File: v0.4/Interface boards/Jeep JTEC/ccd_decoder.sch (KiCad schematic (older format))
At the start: 10 parts, among them Q1 AO3400, Q2 IRF7317

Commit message: Draw Jeep igniters and cruise control drivers
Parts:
- added C? (x2): 3.3n, symbol Device:C
- added JP? (x2): NO, symbol Device:Jumper_NO_Small
- added R? (x2): 10, symbol Device:R
- added R? (x2): 13k, symbol Device:R
- added R?: 120, symbol Device:R
- added U?: USBLC6-2P6, Package_TO_SOT_SMD:SOT-666, symbol Power_Protection:USBLC6-2P6
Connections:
- net CCD+: now also JP?.2, U?.6 (I/O1)
- net CCD-: now also JP?.2, U?.4 (I/O2)
- net CCD_SAFE+: now also C?.1, R?.2
- net CCD_SAFE-: now also C?.1, R?.1
- net GNDA: now also C?.2, C?.2, R?.2, U?.2 (GND)
- net VDDA: now also R?.1, U?.5 (VBUS)
- new net: R?.1, U?.1 (I/O1)
- new net: R?.2, U?.3 (I/O2)
- new net: JP?.1, R?.1, R?.2 (x2)
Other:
- note added: "CCD Termination"
- moved on the sheet: C?, R?, U?A, U?C

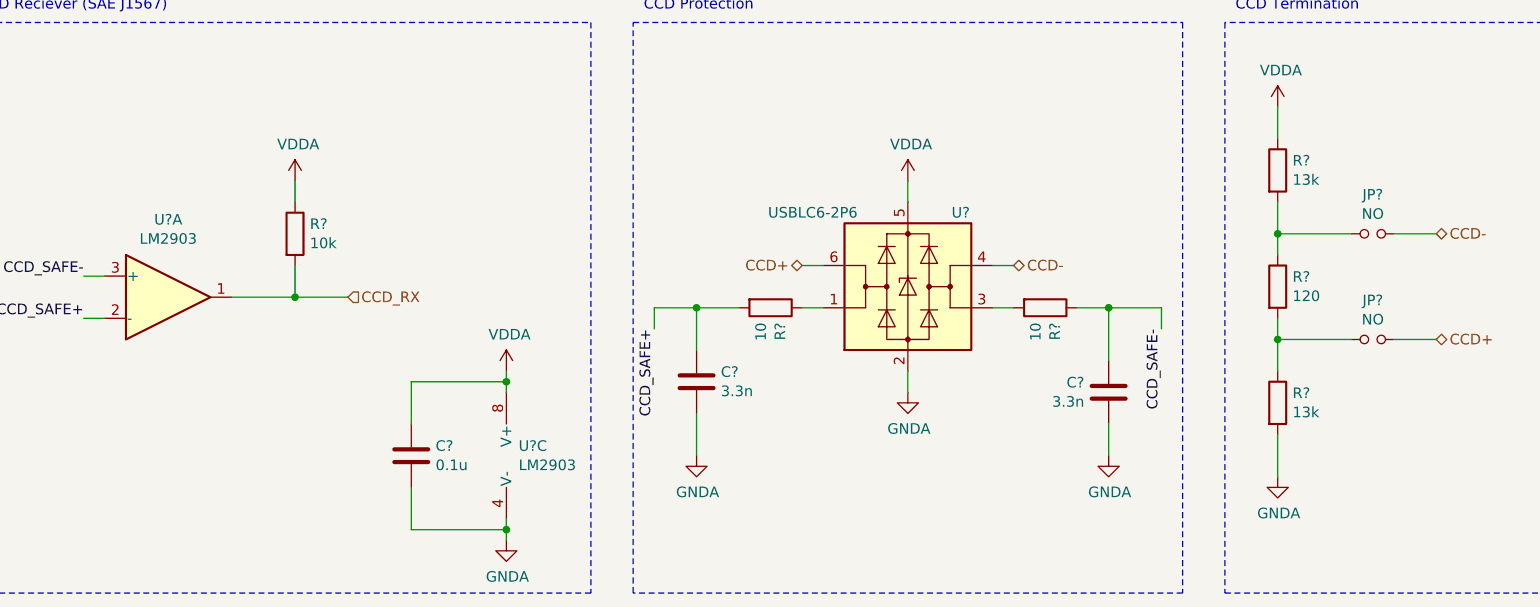
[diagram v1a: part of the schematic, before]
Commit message: Add voltage sense circuit for alternator control
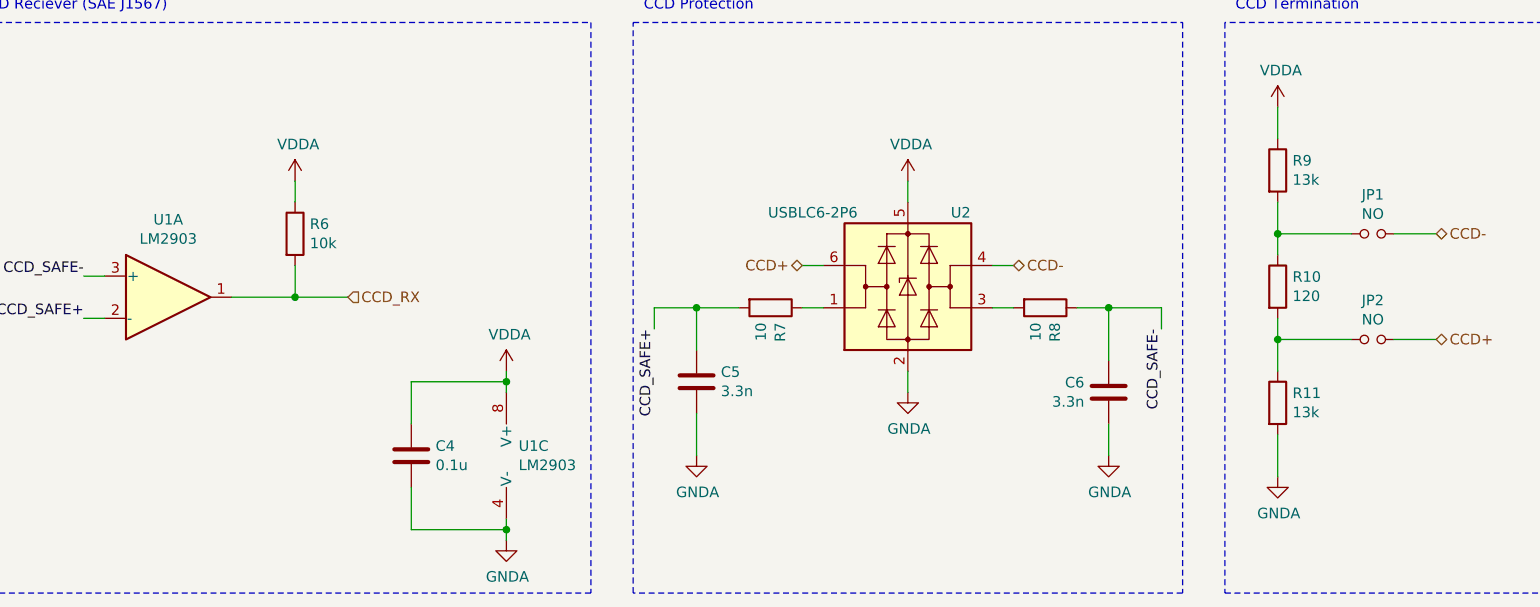
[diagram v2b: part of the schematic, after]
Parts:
- C4, C5, C6: renamed from C?; footprint (none) -> Capacitor_SMD:C_0805_2012Metric
- JP1, JP2: renamed from JP?; footprint (none) -> Connector_PinHeader_2.54mm:PinHeader_1x02_P2.54mm_Vertical
- R1, R2, R3, R4: footprint (none) -> Resistor_SMD:R_0805_2012Metric
- R10, R11, R6, R7, R8, R9: renamed from R?; footprint (none) -> Resistor_SMD:R_0805_2012Metric
- U1: renamed from U?; footprint (none) -> Package_SO:SOIC-8_3.9x4.9mm_P1.27mm; Manufacturer (none) -> onsemi; Manufacturer# (none) -> LM2903DR2G; digikey# (none) -> LM2903DR2GOSCT-ND
- gave numbers to parts that had none: 1
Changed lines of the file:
@@
 F 0 "R1" H 1220 1396 50  0000 L CNN
 F 1 "10k" H 1220 1305 50  0000 L CNN
-F 2 "" V 1080 1350 50  0001 C CNN
+F 2 "Resistor_SMD:R_0805_2012Metric" V 1080 1350 50  0001 C CNN
 F 3 "~" H 1150 1350 50  0001 C CNN
 	1    1150 1350
@@
 F 0 "R2" H 1770 2146 50  0000 L CNN
 F 1 "10k" H 1770 2055 50  0000 L CNN
-F 2 "" V 1630 2100 50  0001 C CNN
+F 2 "Resistor_SMD:R_0805_2012Metric" V 1630 2100 50  0001 C CNN
 F 3 "~" H 1700 2100 50  0001 C CNN
 	1    1700 2100
@@
 F 0 "R3" V 2600 1900 50  0000 C CNN
 F 1 "360" V 2500 1900 50  0000 C CNN
-F 2 "" V 2530 1900 50  0001 C CNN
+F 2 "Resistor_SMD:R_0805_2012Metric" V 2530 1900 50  0001 C CNN
 F 3 "~" H 2600 1900 50  0001 C CNN
 	1    2600 1900
@@
 F 0 "R4" V 2600 2100 50  0000 C CNN
 F 1 "360" V 2500 2100 50  0000 C CNN
-F 2 "" V 2530 2100 50  0001 C CNN
+F 2 "Resistor_SMD:R_0805_2012Metric" V 2530 2100 50  0001 C CNN
 F 3 "~" H 2600 2100 50  0001 C CNN
 	1    2600 2100
@@
 CCD Reciever (SAE J1567)
 $Comp
-L Comparator:LM2903 U?
+L Comparator:LM2903 U1
 U 1 1 61616774
 P 4550 2000
-F 0 "U?" H 4550 2367 50  0000 C CNN
+F 0 "U1" H 4550 2367 50  0000 C CNN
 F 1 "LM2903" H 4550 2276 50  0000 C CNN
-F 2 "" H 4550 2000 50  0001 C CNN
+F 2 "Package_SO:SOIC-8_3.9x4.9mm_P1.27mm" H 4550 2000 50  0001 C CNN
 F 3 "http://www.ti.com/lit/ds/symlink/lm393.pdf" H 4550 2000 50  0001 C CNN
+F 4 "onsemi" H 4550 2000 50  0001 C CNN "Manufacturer"
+F 5 "LM2903DR2G" H 4550 2000 50  0001 C CNN "Manufacturer#"
+F 6 "LM2903DR2GOSCT-ND" H 4550 2000 50  0001 C CNN "digikey#"
 	1    4550 2000
 	1    0    0    -1
 $EndComp
 $Comp
-L Comparator:LM2903 U?
+L Comparator:LM2903 U1
 U 3 1 61617337
 P 6250 2750
-F 0 "U?" H 6208 2796 50  0000 L CNN
+F 0 "U1" H 6208 2796 50  0000 L CNN
 F 1 "LM2903" H 6208 2705 50  0000 L CNN
-F 2 "" H 6250 2750 50  0001 C CNN
+F 2 "Package_SO:SOIC-8_3.9x4.9mm_P1.27mm" H 6250 2750 50  0001 C CNN
 F 3 "http://www.ti.com/lit/ds/symlink/lm393.pdf" H 6250 2750 50  0001 C CNN
+F 4 "onsemi" H 6250 2750 50  0001 C CNN "Manufacturer"
+F 5 "LM2903DR2G" H 6250 2750 50  0001 C CNN "Manufacturer#"
+F 6 "LM2903DR2GOSCT-ND" H 6250 2750 50  0001 C CNN "digikey#"
 	3    6250 2750
 	1    0    0    -1
 $EndComp
 $Comp
-L power:GNDA #PWR?
+L power:GNDA #PWR020
 U 1 1 616184B3
 P 6150 3150
-F 0 "#PWR?" H 6150 2900 50  0001 C CNN
+F 0 "#PWR020" H 6150 2900 50  0001 C CNN
 F 1 "GNDA" H 6155 2977 50  0000 C CNN
 F 2 "" H 6150 3150 50  0001 C CNN
@@
 	6150 2450 6150 2400
 $Comp
-L power:VDDA #PWR?
+L power:VDDA #PWR019
 U 1 1 6161AD97
 P 6150 2350
-F 0 "#PWR?" H 6150 2200 50  0001 C CNN
+F 0 "#PWR019" H 6150 2200 50  0001 C CNN
 F 1 "VDDA" H 6165 2523 50  0000 C CNN
 F 2 "" H 6150 2350 50  0001 C CNN
@@
 $EndComp
 $Comp
-L Device:C C?
+L Device:C C4
 U 1 1 6161B93A
 P 5700 2750
-F 0 "C?" H 5815 2796 50  0000 L CNN
+F 0 "C4" H 5815 2796 50  0000 L CNN
 F 1 "0.1u" H 5815 2705 50  0000 L CNN
-F 2 "" H 5738 2600 50  0001 C CNN
+F 2 "Capacitor_SMD:C_0805_2012Metric" H 5738 2600 50  0001 C CNN
 F 3 "~" H 5700 2750 50  0001 C CNN
 	1    5700 2750
@@
 CCD_RX
 $Comp
-L power:VDDA #PWR?
+L power:VDDA #PWR018
 U 1 1 6161E78E
 P 5150 1450
-F 0 "#PWR?" H 5150 1300 50  0001 C CNN
+F 0 "#PWR018" H 5150 1300 50  0001 C CNN
 F 1 "VDDA" H 5165 1623 50  0000 C CNN
 F 2 "" H 5150 1450 50  0001 C CNN
@@
 $EndComp
 $Comp
-L Device:R R?
+L Device:R R6
 U 1 1 6161EDB4
 P 5150 1700
-F 0 "R?" H 5220 1746 50  0000 L CNN
+F 0 "R6" H 5220 1746 50  0000 L CNN
 F 1 "10k" H 5220 1655 50  0000 L CNN
-F 2 "" V 5080 1700 50  0001 C CNN
+F 2 "Resistor_SMD:R_0805_2012Metric" V 5080 1700 50  0001 C CNN
 F 3 "~" H 5150 1700 50  0001 C CNN
 	1    5150 1700
@@
 CCD_SAFE-
 $Comp
-L Power_Protection:USBLC6-2P6 U?
+L Power_Protection:USBLC6-2P6 U2
 U 1 1 615A235D
 P 8050 1950
-F 0 "U?" H 8300 2300 50  0000 C CNN
+F 0 "U2" H 8300 2300 50  0000 C CNN
 F 1 "USBLC6-2P6" H 7600 2300 50  0000 C CNN
 F 2 "Package_TO_SOT_SMD:SOT-666" H 8050 1450 50  0001 C CNN
@@
 	8450 1850 8550 1850
 $Comp
-L power:GNDA #PWR?
+L power:GNDA #PWR023
 U 1 1 615A5C3E
 P 8050 2450
-F 0 "#PWR?" H 8050 2200 50  0001 C CNN
+F 0 "#PWR023" H 8050 2200 50  0001 C CNN
 F 1 "GNDA" H 8055 2277 50  0000 C CNN
 F 2 "" H 8050 2450 50  0001 C CNN
@@
 	8050 2450 8050 2350
 $Comp
-L power:VDDA #PWR?
+L power:VDDA #PWR022
 U 1 1 615A6B1C
 P 8050 1450
-F 0 "#PWR?" H 8050 1300 50  0001 C CNN
+F 0 "#PWR022" H 8050 1300 50  0001 C CNN
 F 1 "VDDA" H 8065 1623 50  0000 C CNN
 F 2 "" H 8050 1450 50  0001 C CNN
@@
 CCD_SAFE+
 $Comp
-L Device:R R?
+L Device:R R7
 U 1 1 615AC862
 P 7400 2050
-F 0 "R?" H 7470 2096 50  0000 L CNN
+F 0 "R7" H 7470 2096 50  0000 L CNN
 F 1 "10" H 7470 2005 50  0000 L CNN
-F 2 "" V 7330 2050 50  0001 C CNN
+F 2 "Resistor_SMD:R_0805_2012Metric" V 7330 2050 50  0001 C CNN
 F 3 "~" H 7400 2050 50  0001 C CNN
 	1    7400 2050
@@
 	7250 2050 7050 2050
 $Comp
-L Device:R R?
+L Device:R R8
 U 1 1 615ADDE0
 P 8700 2050
-F 0 "R?" H 8770 2096 50  0000 L CNN
+F 0 "R8" H 8770 2096 50  0000 L CNN
 F 1 "10" H 8770 2005 50  0000 L CNN
-F 2 "" V 8630 2050 50  0001 C CNN
+F 2 "Resistor_SMD:R_0805_2012Metric" V 8630 2050 50  0001 C CNN
 F 3 "~" H 8700 2050 50  0001 C CNN
 	1    8700 2050
@@
 CCD Termination
 $Comp
-L power:VDDA #PWR?
+L power:VDDA #PWR025
 U 1 1 615B212E
 P 9800 1100
-F 0 "#PWR?" H 9800 950 50  0001 C CNN
+F 0 "#PWR025" H 9800 950 50  0001 C CNN
 F 1 "VDDA" H 9815 1273 50  0000 C CNN
 F 2 "" H 9800 1100 50  0001 C CNN
@@
 $EndComp
 $Comp
-L power:GNDA #PWR?
+L power:GNDA #PWR026
 U 1 1 615B2717
 P 9800 2850
-F 0 "#PWR?" H 9800 2600 50  0001 C CNN
+F 0 "#PWR026" H 9800 2600 50  0001 C CNN
 F 1 "GNDA" H 9805 2677 50  0000 C CNN
 F 2 "" H 9800 2850 50  0001 C CNN
@@
 	9800 2850 9800 2650
 $Comp
-L Device:R R?
+L Device:R R9
 U 1 1 615B365D
 P 9800 1400
-F 0 "R?" H 9870 1446 50  0000 L CNN
+F 0 "R9" H 9870 1446 50  0000 L CNN
 F 1 "13k" H 9870 1355 50  0000 L CNN
-F 2 "" V 9730 1400 50  0001 C CNN
+F 2 "Resistor_SMD:R_0805_2012Metric" V 9730 1400 50  0001 C CNN
 F 3 "~" H 9800 1400 50  0001 C CNN
 	1    9800 1400
@@
 	9800 1250 9800 1100
 $Comp
-L Device:R R?
+L Device:R R10
 U 1 1 615B3B7C
 P 9800 1950
-F 0 "R?" H 9870 1996 50  0000 L CNN
+F 0 "R10" H 9870 1996 50  0000 L CNN
 F 1 "120" H 9870 1905 50  0000 L CNN
-F 2 "" V 9730 1950 50  0001 C CNN
+F 2 "Resistor_SMD:R_0805_2012Metric" V 9730 1950 50  0001 C CNN
 F 3 "~" H 9800 1950 50  0001 C CNN
 	1    9800 1950
@@
 	9800 1800 9800 1700
 $Comp
-L Device:R R?
+L Device:R R11
 U 1 1 615B3F0E
 P 9800 2500
-F 0 "R?" H 9870 2546 50  0000 L CNN
+F 0 "R11" H 9870 2546 50  0000 L CNN
 F 1 "13k" H 9870 2455 50  0000 L CNN
-F 2 "" V 9730 2500 50  0001 C CNN
+F 2 "Resistor_SMD:R_0805_2012Metric" V 9730 2500 50  0001 C CNN
 F 3 "~" H 9800 2500 50  0001 C CNN
 	1    9800 2500
@@
 CCD+
 $Comp
-L Device:Jumper_NO_Small JP?
+L Device:Jumper_NO_Small JP1
 U 1 1 615B6D01
 P 10250 1700
-F 0 "JP?" H 10250 1885 50  0000 C CNN
+F 0 "JP1" H 10250 1885 50  0000 C CNN
 F 1 "NO" H 10250 1794 50  0000 C CNN
-F 2 "" H 10250 1700 50  0001 C CNN
+F 2 "Connector_PinHeader_2.54mm:PinHeader_1x02_P2.54mm_Vertical" H 10250 1700 50  0001 C CNN
 F 3 "~" H 10250 1700 50  0001 C CNN
 	1    10250 1700
@@
 	10350 1700 10550 1700
 $Comp
-L Device:Jumper_NO_Small JP?
+L Device:Jumper_NO_Small JP2
 U 1 1 615B7377
 P 10250 2200
-F 0 "JP?" H 10250 2385 50  0000 C CNN
+F 0 "JP2" H 10250 2385 50  0000 C CNN
 F 1 "NO" H 10250 2294 50  0000 C CNN
-F 2 "" H 10250 2200 50  0001 C CNN
+F 2 "Connector_PinHeader_2.54mm:PinHeader_1x02_P2.54mm_Vertical" H 10250 2200 50  0001 C CNN
 F 3 "~" H 10250 2200 50  0001 C CNN
 	1    10250 2200
@@
 	10350 2200 10550 2200
 $Comp
-L Device:C C?
+L Device:C C5
 U 1 1 615B9890
 P 7050 2400
-F 0 "C?" H 7165 2446 50  0000 L CNN
+F 0 "C5" H 7165 2446 50  0000 L CNN
 F 1 "3.3n" H 7165 2355 50  0000 L CNN
-F 2 "" H 7088 2250 50  0001 C CNN
+F 2 "Capacitor_SMD:C_0805_2012Metric" H 7088 2250 50  0001 C CNN
 F 3 "~" H 7050 2400 50  0001 C CNN
 	1    7050 2400
@@
 	7050 2050 6850 2050
 $Comp
-L Device:C C?
+L Device:C C6
 U 1 1 615B9D00
 P 9000 2450
-F 0 "C?" H 9115 2496 50  0000 L CNN
+F 0 "C6" H 9115 2496 50  0000 L CNN
 F 1 "3.3n" H 9115 2405 50  0000 L CNN
-F 2 "" H 9038 2300 50  0001 C CNN
+F 2 "Capacitor_SMD:C_0805_2012Metric" H 9038 2300 50  0001 C CNN
 F 3 "~" H 9000 2450 50  0001 C CNN
 	1    9000 2450
@@
 	9000 2050 9250 2050
 $Comp
-L power:GNDA #PWR?
+L power:GNDA #PWR021
 U 1 1 615BCDBA
 P 7050 2750
-F 0 "#PWR?" H 7050 2500 50  0001 C CNN
+F 0 "#PWR021" H 7050 2500 50  0001 C CNN
 F 1 "GNDA" H 7055 2577 50  0000 C CNN
 F 2 "" H 7050 2750 50  0001 C CNN
@@
 $EndComp
 $Comp
-L power:GNDA #PWR?
+L power:GNDA #PWR024
 U 1 1 615BD076
 P 9000 2750
-F 0 "#PWR?" H 9000 2500 50  0001 C CNN
+F 0 "#PWR024" H 9000 2500 50  0001 C CNN
 F 1 "GNDA" H 9005 2577 50  0000 C CNN
 F 2 "" H 9000 2750 50  0001 C CNN

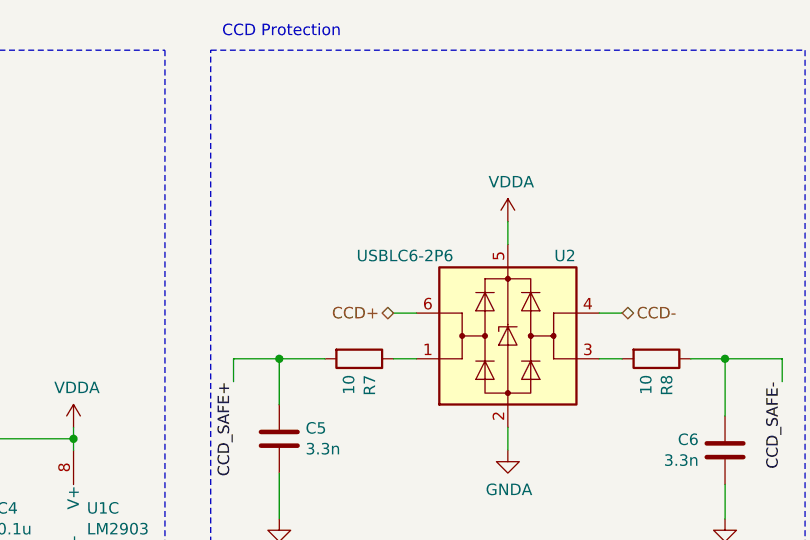
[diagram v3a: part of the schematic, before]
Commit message: Add BOM items for jellybean parts
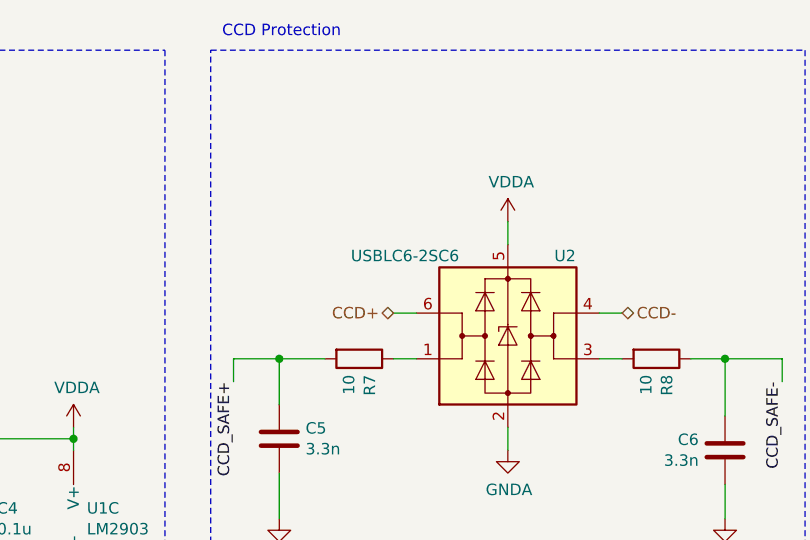
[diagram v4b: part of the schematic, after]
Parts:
- C4: Manufacturer (none) -> Kemet; Manufacturer# (none) -> C0805C104K5RACTU
- C5, C6: Manufacturer (none) -> TDK; Manufacturer# (none) -> C2012C0G1H332J060AA
- JP1, JP2: Manufacturer (none) -> 10129378-902001BLF; Manufacturer# (none) -> Amphenol ICC (FCI); digikey# (none) -> 10129378-902001BLF-ND
- Q2: Manufacturer (none) -> Infineon; Manufacturer# (none) -> IRF7317TRPBF
- R1, R2, R6: Manufacturer (none) -> Yageo; Manufacturer# (none) -> RC0805FR-0710KL
- R10: Manufacturer (none) -> Panasonic; Manufacturer# (none) -> ERJP6WF1200V
- R11, R9: Manufacturer (none) -> Panasonic; Manufacturer# (none) -> ERJ-6ENF1302V
- R3, R4: Manufacturer (none) -> Yageo; Manufacturer# (none) -> RC0805JR-07360RL
- R7, R8: Manufacturer (none) -> Yageo; Manufacturer# (none) -> RC0805FR-0710RL
- U2: value USBLC6-2P6 -> USBLC6-2SC6; Manufacturer (none) -> STMicroelectronics; Manufacturer# (none) -> USBLC6-2SC6
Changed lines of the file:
@@
 EESchema Schematic File Version 4
+LIBS:Jeep JTEC-cache
 EELAYER 30 0
 EELAYER END
@@
 F 2 "Resistor_SMD:R_0805_2012Metric" V 1080 1350 50  0001 C CNN
 F 3 "~" H 1150 1350 50  0001 C CNN
+F 4 "Yageo" H 1150 1350 50  0001 C CNN "Manufacturer"
+F 5 "RC0805FR-0710KL" H 1150 1350 50  0001 C CNN "Manufacturer#"
 	1    1150 1350
 	1    0    0    -1
@@
 F 2 "Package_SO:SOIC-8_3.9x4.9mm_P1.27mm" H 2400 1525 50  0001 L CNN
 F 3 "http://www.irf.com/product-info/datasheets/data/irf7309ipbf.pdf" H 2300 1600 50  0001 L CNN
+F 4 "Infineon" H 2200 1600 50  0001 C CNN "Manufacturer"
+F 5 "IRF7317TRPBF" H 2200 1600 50  0001 C CNN "Manufacturer#"
 	2    2200 1600
 	1    0    0    1
@@
 F 2 "Package_SO:SOIC-8_3.9x4.9mm_P1.27mm" H 2400 2325 50  0001 L CNN
 F 3 "http://www.irf.com/product-info/datasheets/data/irf7309ipbf.pdf" H 2300 2400 50  0001 L CNN
+F 4 "Infineon" H 2200 2400 50  0001 C CNN "Manufacturer"
+F 5 "IRF7317TRPBF" H 2200 2400 50  0001 C CNN "Manufacturer#"
 	1    2200 2400
 	1    0    0    -1
@@
 F 2 "Resistor_SMD:R_0805_2012Metric" V 1630 2100 50  0001 C CNN
 F 3 "~" H 1700 2100 50  0001 C CNN
+F 4 "Yageo" H 1700 2100 50  0001 C CNN "Manufacturer"
+F 5 "RC0805FR-0710KL" H 1700 2100 50  0001 C CNN "Manufacturer#"
 	1    1700 2100
 	1    0    0    -1
@@
 F 2 "Resistor_SMD:R_0805_2012Metric" V 2530 1900 50  0001 C CNN
 F 3 "~" H 2600 1900 50  0001 C CNN
+F 4 "Yageo" H 2600 1900 50  0001 C CNN "Manufacturer"
+F 5 "RC0805JR-07360RL" H 2600 1900 50  0001 C CNN "Manufacturer#"
 	1    2600 1900
 	0    1    1    0
@@
 F 2 "Resistor_SMD:R_0805_2012Metric" V 2530 2100 50  0001 C CNN
 F 3 "~" H 2600 2100 50  0001 C CNN
+F 4 "Yageo" H 2600 2100 50  0001 C CNN "Manufacturer"
+F 5 "RC0805JR-07360RL" H 2600 2100 50  0001 C CNN "Manufacturer#"
 	1    2600 2100
 	0    1    -1   0
@@
 F 2 "Capacitor_SMD:C_0805_2012Metric" H 5738 2600 50  0001 C CNN
 F 3 "~" H 5700 2750 50  0001 C CNN
+F 4 "Kemet" H 5700 2750 50  0001 C CNN "Manufacturer"
+F 5 "C0805C104K5RACTU" H 5700 2750 50  0001 C CNN "Manufacturer#"
 	1    5700 2750
 	1    0    0    -1
@@
 F 2 "Resistor_SMD:R_0805_2012Metric" V 5080 1700 50  0001 C CNN
 F 3 "~" H 5150 1700 50  0001 C CNN
+F 4 "Yageo" H 5150 1700 50  0001 C CNN "Manufacturer"
+F 5 "RC0805FR-0710KL" H 5150 1700 50  0001 C CNN "Manufacturer#"
 	1    5150 1700
 	1    0    0    -1
@@
 P 8050 1950
 F 0 "U2" H 8300 2300 50  0000 C CNN
-F 1 "USBLC6-2P6" H 7600 2300 50  0000 C CNN
+F 1 "USBLC6-2SC6" H 7600 2300 50  0000 C CNN
 F 2 "Package_TO_SOT_SMD:SOT-666" H 8050 1450 50  0001 C CNN
 F 3 "https://www.st.com/resource/en/datasheet/usblc6-2.pdf" H 8250 2300 50  0001 C CNN
+F 4 "STMicroelectronics" H 8050 1950 50  0001 C CNN "Manufacturer"
+F 5 "USBLC6-2SC6" H 8050 1950 50  0001 C CNN "Manufacturer#"
 	1    8050 1950
 	1    0    0    -1
@@
 F 2 "Resistor_SMD:R_0805_2012Metric" V 7330 2050 50  0001 C CNN
 F 3 "~" H 7400 2050 50  0001 C CNN
+F 4 "Yageo" H 7400 2050 50  0001 C CNN "Manufacturer"
+F 5 "RC0805FR-0710RL" H 7400 2050 50  0001 C CNN "Manufacturer#"
 	1    7400 2050
 	0    1    1    0
@@
 F 2 "Resistor_SMD:R_0805_2012Metric" V 8630 2050 50  0001 C CNN
 F 3 "~" H 8700 2050 50  0001 C CNN
+F 4 "Yageo" H 8700 2050 50  0001 C CNN "Manufacturer"
+F 5 "RC0805FR-0710RL" H 8700 2050 50  0001 C CNN "Manufacturer#"
 	1    8700 2050
 	0    1    1    0
@@
 F 2 "Resistor_SMD:R_0805_2012Metric" V 9730 1400 50  0001 C CNN
 F 3 "~" H 9800 1400 50  0001 C CNN
+F 4 "Panasonic" H 9800 1400 50  0001 C CNN "Manufacturer"
+F 5 "ERJ-6ENF1302V" H 9800 1400 50  0001 C CNN "Manufacturer#"
 	1    9800 1400
 	1    0    0    -1
@@
 F 2 "Resistor_SMD:R_0805_2012Metric" V 9730 1950 50  0001 C CNN
 F 3 "~" H 9800 1950 50  0001 C CNN
+F 4 "Panasonic" H 9800 1950 50  0001 C CNN "Manufacturer"
+F 5 "ERJP6WF1200V" H 9800 1950 50  0001 C CNN "Manufacturer#"
 	1    9800 1950
 	1    0    0    -1
@@
 F 2 "Resistor_SMD:R_0805_2012Metric" V 9730 2500 50  0001 C CNN
 F 3 "~" H 9800 2500 50  0001 C CNN
+F 4 "Panasonic" H 9800 2500 50  0001 C CNN "Manufacturer"
+F 5 "ERJ-6ENF1302V" H 9800 2500 50  0001 C CNN "Manufacturer#"
 	1    9800 2500
 	1    0    0    -1
@@
 F 2 "Connector_PinHeader_2.54mm:PinHeader_1x02_P2.54mm_Vertical" H 10250 1700 50  0001 C CNN
 F 3 "~" H 10250 1700 50  0001 C CNN
+F 4 "10129378-902001BLF" H 10250 1700 50  0001 C CNN "Manufacturer"
+F 5 "Amphenol ICC (FCI)" H 10250 1700 50  0001 C CNN "Manufacturer#"
+F 6 "10129378-902001BLF-ND" H 10250 1700 50  0001 C CNN "digikey#"
 	1    10250 1700
 	1    0    0    -1
@@
 F 2 "Connector_PinHeader_2.54mm:PinHeader_1x02_P2.54mm_Vertical" H 10250 2200 50  0001 C CNN
 F 3 "~" H 10250 2200 50  0001 C CNN
+F 4 "10129378-902001BLF" H 10250 2200 50  0001 C CNN "Manufacturer"
+F 5 "Amphenol ICC (FCI)" H 10250 2200 50  0001 C CNN "Manufacturer#"
+F 6 "10129378-902001BLF-ND" H 10250 2200 50  0001 C CNN "digikey#"
 	1    10250 2200
 	1    0    0    -1
@@
 F 2 "Capacitor_SMD:C_0805_2012Metric" H 7088 2250 50  0001 C CNN
 F 3 "~" H 7050 2400 50  0001 C CNN
+F 4 "TDK" H 7050 2400 50  0001 C CNN "Manufacturer"
+F 5 "C2012C0G1H332J060AA" H 7050 2400 50  0001 C CNN "Manufacturer#"
 	1    7050 2400
 	1    0    0    -1
@@
 F 2 "Capacitor_SMD:C_0805_2012Metric" H 9038 2300 50  0001 C CNN
 F 3 "~" H 9000 2450 50  0001 C CNN
+F 4 "TDK" H 9000 2450 50  0001 C CNN "Manufacturer"
+F 5 "C2012C0G1H332J060AA" H 9000 2450 50  0001 C CNN "Manufacturer#"
 	1    9000 2450
 	-1   0    0    -1

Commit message: Correct the footprint for U2
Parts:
- U2: footprint Package_TO_SOT_SMD:SOT-666 -> Package_TO_SOT_SMD:SOT-23-6
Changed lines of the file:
@@
 F 0 "U2" H 8300 2300 50  0000 C CNN
 F 1 "USBLC6-2SC6" H 7600 2300 50  0000 C CNN
-F 2 "Package_TO_SOT_SMD:SOT-666" H 8050 1450 50  0001 C CNN
+F 2 "Package_TO_SOT_SMD:SOT-23-6" H 8050 1450 50  0001 C CNN
 F 3 "https://www.st.com/resource/en/datasheet/usblc6-2.pdf" H 8250 2300 50  0001 C CNN
 F 4 "STMicroelectronics" H 8050 1950 50  0001 C CNN "Manufacturer"
